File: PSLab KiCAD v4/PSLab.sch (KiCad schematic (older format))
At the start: 79 parts, among them CON1 USB-MINI-B, J1 Programmer, J10 GND, J11 Vbus, J12 Sensors, J13 D+, J14 D-, J2 SQRs, J3 LA, J4 OSC_Pins, J6 I2C, J7 IDs, J8 TX_RX_ES, J9 Test_Vs, P7 NRF, Q2 MMBT3904, Q3 MMBT3906, U1 MCP2200, U15 ESP8266, U2 74HC126, U3 PIC24EP256GP204, U4 TC1240A, U5 7660, U6 LM1117-3.3, X1 12MHz, Y1 12MHz

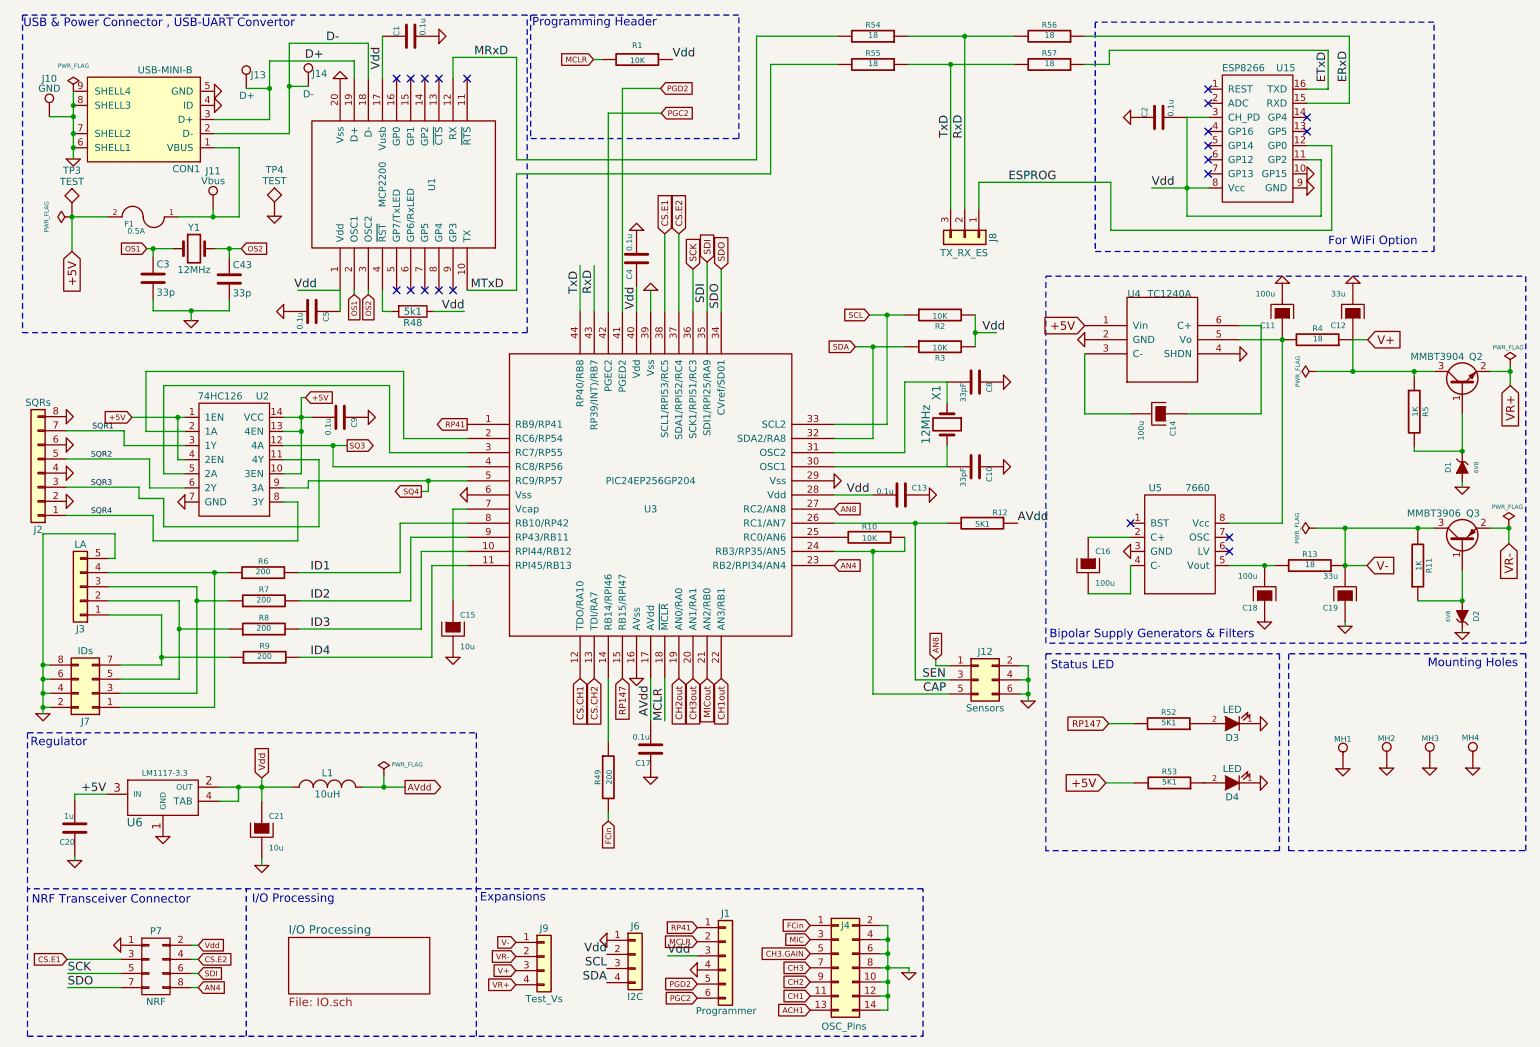
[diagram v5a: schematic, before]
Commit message: New layout with pins adjusted + Bluetooth
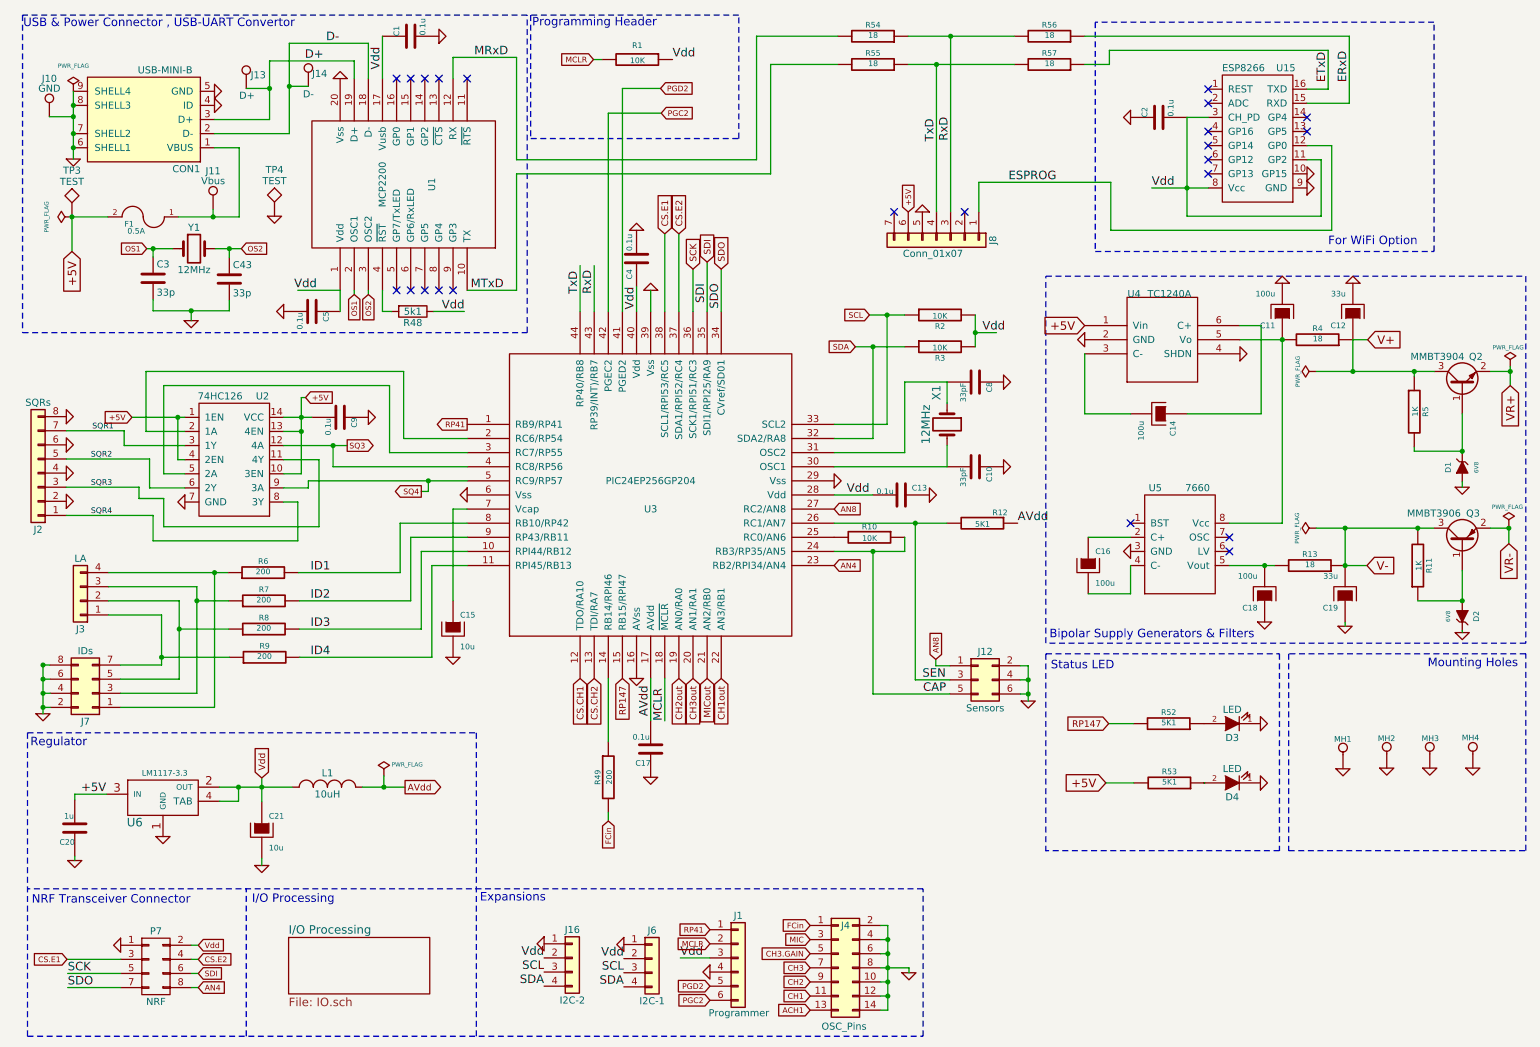
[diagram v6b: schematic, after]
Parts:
- removed J3: LA, Pin_Headers:Pin_Header_Straight_1x05_Pitch2.54mm, symbol Conn_01x05
- removed J8: TX_RX_ES, Pin_Headers:Pin_Header_Straight_1x03_Pitch2.54mm, symbol Conn_01x03
- removed J9: Test_Vs, Pin_Headers:Pin_Header_Straight_1x04_Pitch2.54mm, symbol Conn_01x04
- added J16: I2C-2, Pin_Headers:Pin_Header_Straight_1x04_Pitch2.54mm, symbol Conn_01x04
- added J3: LA, Pin_Headers:Pin_Header_Straight_1x04_Pitch2.54mm, symbol Conn_01x04
- added J8: Conn_01x07, Pin_Headers:Pin_Header_Straight_1x07_Pitch2.54mm, symbol Conn_01x07
- J6: value I2C -> I2C-1
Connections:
- net +5V: now also J8.6 (Pin_6)
- net ESPROG: now also J8.1 (Pin_1)
- net GND: now also J16.1 (Pin_1), J8.5 (Pin_5)
- net RxD: now also J8.3 (Pin_3)
- net SCL: now also J16.3 (Pin_3)
- net SDA: now also J16.4 (Pin_4)
- net TxD: now also J8.4 (Pin_4)
- net Vdd: now also J16.2 (Pin_2)
- net at J7.3 (Pin_3), R7.1: now also J3.3 (Pin_3)
- net at J7.1 (Pin_1), R6.1: now also J3.4 (Pin_4)
- net at J7.5 (Pin_5), R8.1: now also J3.2 (Pin_2)
- net at J7.7 (Pin_7), R9.1: now also J3.1 (Pin_1)
- no-connect marks 21 -> 23
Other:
- moved on the sheet: J1, J6
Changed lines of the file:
@@
 Text GLabel 6080 7150 0    40   Input ~ 0
 CH3.GAIN
-Text Label 4640 7355 2    60   ~ 0
+Text Label 4760 7385 2    60   ~ 0
 SDA
-Text Label 4640 7255 2    60   ~ 0
+Text Label 4760 7285 2    60   ~ 0
 SCL
 $Comp
 L GND-RESCUE-proto1 #PWR033
 U 1 1 55B40810
-P 4640 7055
-F 0 "#PWR033" H 4640 7055 30  0001 C CNN
-F 1 "GND" H 4640 6985 30  0001 C CNN
-F 2 "" H 4640 7055 60  0000 C CNN
-F 3 "" H 4640 7055 60  0000 C CNN
-	1    4640 7055
+P 4760 7085
+F 0 "#PWR033" H 4760 7085 30  0001 C CNN
+F 1 "GND" H 4760 7015 30  0001 C CNN
+F 2 "" H 4760 7085 60  0000 C CNN
+F 3 "" H 4760 7085 60  0000 C CNN
+	1    4760 7085
 	0    1    1    0
 $EndComp
-Text Label 4640 7155 2    60   ~ 0
-Vdd
 $Comp
 L Crystal X1
@@
 Text GLabel 5020 1020 2    40   Input ~ 0
 PGD2
-Text GLabel 5280 7365 0    40   Input ~ 0
+Text GLabel 5370 7380 0    40   Input ~ 0
 PGD2
-Text GLabel 5280 7465 0    40   Input ~ 0
+Text GLabel 5370 7480 0    40   Input ~ 0
 PGC2
 $Comp
@@
 Text GLabel 11040 3125 3    60   Input ~ 0
 VR+
-Text GLabel 5280 6965 0    40   Input ~ 0
+Text GLabel 5370 6980 0    40   Input ~ 0
 RP41
 Text GLabel 6970 5065 1    40   Input ~ 0
@@
 Text GLabel 3210 5970 2    47   Output ~ 0
 AVdd
-Text Label 7175 1375 1    60   ~ 0
+Text Label 7075 1390 1    60   ~ 0
 RxD
-Text Label 7075 1370 1    60   ~ 0
+Text Label 6975 1395 1    60   ~ 0
 TxD
 Text GLabel 3325 3875 0    40   Output ~ 0
@@
 	0    -1   -1   0
 $EndComp
-$Comp
-L Conn_01x03 J8
-U 1 1 5A320F8A
-P 7175 2075
-F 0 "J8" H 7175 2275 50  0000 C CNN
-F 1 "TX_RX_ES" V 7285 2070 50  0000 C CNN
-F 2 "Pin_Headers:Pin_Header_Straight_1x03_Pitch2.54mm" H 7175 2075 50  0001 C CNN
-F 3 "" H 7175 2075 50  0001 C CNN
-	1    7175 2075
-	0    1    1    0
-$EndComp
 Text Label 7485 1685 0    60   ~ 0
 ESPROG
@@
 L Conn_01x06 J1
 U 1 1 5A56B55E
-P 5480 7165
-F 0 "J1" H 5480 7465 50  0000 C CNN
-F 1 "Programmer" H 5485 6775 50  0000 C CNN
-F 2 "Pin_Headers:Pin_Header_Straight_1x06_Pitch2.54mm" H 5480 7165 50  0001 C CNN
-F 3 "" H 5480 7165 50  0001 C CNN
-	1    5480 7165
-	1    0    0    -1
-$EndComp
-Text Label 5070 7165 0    60   ~ 0
-Vdd
+P 5570 7180
+F 0 "J1" H 5570 7480 50  0000 C CNN
+F 1 "Programmer" H 5575 6790 50  0000 C CNN
+F 2 "Pin_Headers:Pin_Header_Straight_1x06_Pitch2.54mm" H 5570 7180 50  0001 C CNN
+F 3 "" H 5570 7180 50  0001 C CNN
+	1    5570 7180
+	1    0    0    -1
+$EndComp
 $Comp
 L GND-RESCUE-proto1 #PWR048
 U 1 1 5A56D115
-P 5280 7265
-F 0 "#PWR048" H 5280 7265 30  0001 C CNN
-F 1 "GND" H 5280 7195 30  0001 C CNN
-F 2 "" H 5280 7265 60  0000 C CNN
-F 3 "" H 5280 7265 60  0000 C CNN
-	1    5280 7265
+P 5370 7280
+F 0 "#PWR048" H 5370 7280 30  0001 C CNN
+F 1 "GND" H 5370 7210 30  0001 C CNN
+F 2 "" H 5370 7280 60  0000 C CNN
+F 3 "" H 5370 7280 60  0000 C CNN
+	1    5370 7280
 	0    1    1    0
 $EndComp
-Text GLabel 5280 7065 0    40   Input ~ 0
+Text GLabel 5370 7080 0    40   Input ~ 0
 MCLR
 Text GLabel 4545 815  0    40   Input ~ 0
@@
 L Conn_01x04 J6
 U 1 1 5A584DF9
-P 4840 7155
-F 0 "J6" H 4840 7355 50  0000 C CNN
-F 1 "I2C" H 4840 6855 50  0000 C CNN
-F 2 "Pin_Headers:Pin_Header_Straight_1x04_Pitch2.54mm" H 4840 7155 50  0001 C CNN
-F 3 "" H 4840 7155 50  0001 C CNN
-	1    4840 7155
+P 4960 7185
+F 0 "J6" H 4960 7385 50  0000 C CNN
+F 1 "I2C-1" H 4960 6885 50  0000 C CNN
+F 2 "Pin_Headers:Pin_Header_Straight_1x04_Pitch2.54mm" H 4960 7185 50  0001 C CNN
+F 3 "" H 4960 7185 50  0001 C CNN
+	1    4960 7185
 	1    0    0    -1
 $EndComp
@@
 	1    0    0    -1
 $EndComp
-$Comp
-L Conn_01x04 J9
-U 1 1 5A57CD2F
-P 4195 7170
-F 0 "J9" H 4195 7370 50  0000 C CNN
-F 1 "Test_Vs" H 4195 6870 50  0000 C CNN
-F 2 "Pin_Headers:Pin_Header_Straight_1x04_Pitch2.54mm" H 4195 7170 50  0001 C CNN
-F 3 "" H 4195 7170 50  0001 C CNN
-	1    4195 7170
-	1    0    0    -1
-$EndComp
-Text GLabel 3995 7070 0    40   Input ~ 0
-V-
-Text GLabel 3995 7170 0    40   Input ~ 0
-VR-
-Text GLabel 3995 7270 0    40   Input ~ 0
-V+
-Text GLabel 3995 7370 0    40   Input ~ 0
-VR+
-$Comp
-L Conn_01x05 J3
-U 1 1 5A595092
-P 910 4550
-F 0 "J3" H 910 4850 50  0000 C CNN
-F 1 "LA" H 910 4250 50  0000 C CNN
-F 2 "Pin_Headers:Pin_Header_Straight_1x05_Pitch2.54mm" H 910 4550 50  0001 C CNN
-F 3 "" H 910 4550 50  0001 C CNN
-	1    910  4550
-	-1   0    0    1
-$EndComp
 Wire Wire Line
 	3400 4400 3650 4400
@@
 	8175 5940 8375 5940
 Wire Wire Line
-	7275 1875 7275 1685
+	7275 1685 7275 1895
 Wire Wire Line
 	7275 1685 8210 1685
-Wire Wire Line
-	7175 1875 7175 650
-Connection ~ 7175 650
-Wire Wire Line
-	7075 1875 7075 850
-Connection ~ 7075 850
 Wire Notes Line
 	10500 550  8100 550
@@
 Wire Wire Line
 	6780 7250 6780 7285
-Wire Wire Line
-	5280 7165 5070 7165
 Wire Wire Line
 	4605 815  4545 815
@@
 	695  5405 645  5405
 Wire Wire Line
-	645  4175 645  5450
-Wire Wire Line
 	645  5105 695  5105
 Wire Wire Line
@@
 Connection ~ 645  5105
 Wire Wire Line
-	1110 4350 1155 4350
-Wire Wire Line
-	1155 4350 1155 4175
-Wire Wire Line
-	1155 4175 645  4175
-Wire Wire Line
 	1110 4450 1955 4450
 Wire Wire Line
@@
 	1485 5105 1195 5105
 Connection ~ 1485 5050
+Text Label 4760 7185 2    60   ~ 0
+Vdd
+Wire Wire Line
+	5370 7180 5160 7180
+Text Label 5160 7180 0    60   ~ 0
+Vdd
+$Comp
+L Conn_01x04 J16
+U 1 1 5AD47B2C
+P 4395 7180
+F 0 "J16" H 4395 7380 50  0000 C CNN
+F 1 "I2C-2" H 4395 6880 50  0000 C CNN
+F 2 "Pin_Headers:Pin_Header_Straight_1x04_Pitch2.54mm" H 4395 7180 50  0001 C CNN
+F 3 "" H 4395 7180 50  0001 C CNN
+	1    4395 7180
+	1    0    0    -1
+$EndComp
+$Comp
+L GND-RESCUE-proto1 #PWR059
+U 1 1 5AD48170
+P 4195 7080
+F 0 "#PWR059" H 4195 7080 30  0001 C CNN
+F 1 "GND" H 4195 7010 30  0001 C CNN
+F 2 "" H 4195 7080 60  0000 C CNN
+F 3 "" H 4195 7080 60  0000 C CNN
+	1    4195 7080
+	0    1    1    0
+$EndComp
+Text Label 4195 7180 2    60   ~ 0
+Vdd
+Text Label 4195 7280 2    60   ~ 0
+SCL
+Text Label 4195 7380 2    60   ~ 0
+SDA
+$Comp
+L Conn_01x07 J8
+U 1 1 5AD486BC
+P 6975 2095
+F 0 "J8" H 6975 2495 50  0000 C CNN
+F 1 "Conn_01x07" V 7070 2070 50  0000 C CNN
+F 2 "Pin_Headers:Pin_Header_Straight_1x07_Pitch2.54mm" H 6975 2095 50  0001 C CNN
+F 3 "" H 6975 2095 50  0001 C CNN
+	1    6975 2095
+	0    1    1    0
+$EndComp
+Wire Wire Line
+	6975 1895 6975 850
+Connection ~ 6975 850
+Wire Wire Line
+	7075 1895 7075 650
+Connection ~ 7075 650
+$Comp
+L GND-RESCUE-proto1 #PWR060
+U 1 1 5AD4BD5F
+P 6875 1895
+F 0 "#PWR060" H 6875 1895 30  0001 C CNN
+F 1 "GND" H 6875 1825 30  0001 C CNN
+F 2 "" H 6875 1895 60  0000 C CNN
+F 3 "" H 6875 1895 60  0000 C CNN
+	1    6875 1895
+	-1   0    0    1
+$EndComp
+Text GLabel 6775 1895 1    40   Input ~ 0
++5V
+NoConn ~ 7175 1895
+NoConn ~ 6675 1895
+$Comp
+L Conn_01x04 J3
+U 1 1 5AD4C0DD
+P 910 4650
+F 0 "J3" H 910 4850 50  0000 C CNN
+F 1 "LA" H 910 4350 50  0000 C CNN
+F 2 "Pin_Headers:Pin_Header_Straight_1x04_Pitch2.54mm" H 910 4650 50  0001 C CNN
+F 3 "" H 910 4650 50  0001 C CNN
+	1    910  4650
+	-1   0    0    1
+$EndComp
+Wire Wire Line
+	645  5105 645  5450
 $EndSCHEMATC

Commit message: Modifications to PSLab PCB (#39)
* Refined BOM Sheet

* Added FOSSASIA Logo and updated BoM

* NRF replaced with Bluetooth

* Modified silk screen texts
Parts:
- removed C15, C21: 10u, Capacitors_SMD:C_0603, symbol CAPAPOL
- removed J12: Sensors, Pin_Headers:Pin_Header_Straight_2x03_Pitch2.54mm, symbol Conn_02x03_Odd_Even
- removed J2: SQRs, Pin_Headers:Pin_Header_Straight_1x08_Pitch2.54mm, symbol Conn_01x08
- removed J4: OSC_Pins, Pin_Headers:Pin_Header_Straight_2x07_Pitch2.54mm, symbol Conn_02x07_Odd_Even
- removed J7: IDs, Pin_Headers:Pin_Header_Straight_2x04_Pitch2.54mm, symbol Conn_02x04_Odd_Even
- removed J8: Conn_01x07, Pin_Headers:Pin_Header_Straight_1x07_Pitch2.54mm, symbol Conn_01x07
- removed P7: NRF, Pin_Headers:Pin_Header_Straight_2x04_Pitch2.54mm, symbol CONN_02X04
- added C15, C21: 10u, Capacitors_SMD:C_0603, symbol C-RESCUE-proto1
- added J2: DoublePins, Pin_Headers:Pin_Header_Straight_2x14_Pitch2.54mm, symbol Conn_02x14_Odd_Even
- added J5: Bluetooth, Pin_Headers:Pin_Header_Straight_1x06_Pitch2.54mm, symbol Conn_01x06
- added J7: UART/ESP, Pin_Headers:Pin_Header_Straight_1x07_Pitch2.54mm, symbol Conn_01x07
- C10, C8: value 33pF -> 33p
- C3, C43: symbol C -> C-RESCUE-proto1
- MH1, MH2, MH3, MH4: footprint Mounting_Holes:MountingHole_2.2mm_M2_ISO14580_Pad -> Mounting_Holes:MountingHole_3.2mm_M3_DIN965_Pad
- R48: value 5k1 -> 5K1; symbol R -> R-RESCUE-proto1
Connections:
- net +5V: now also J5.2 (Pin_2), J7.6 (Pin_6)
- net ACH1: now also J2.19 (Pin_19)
- net AN8: now also J2.1 (Pin_1)
- net CAP: now also J2.5 (Pin_5)
- net CH1: now also J2.17 (Pin_17)
- net CH2: now also J2.15 (Pin_15)
- net CH3: now also J2.13 (Pin_13)
- net CH3.GAIN: now also J2.11 (Pin_11)
- net ESPROG: now also J7.2 (Pin_2)
- net FCin: now also J2.7 (Pin_7)
- net GND: now also J1.3 (Pin_3), C15.1, C21.1, J2.10 (Pin_10), J2.12 (Pin_12), J2.14 (Pin_14), J2.16 (Pin_16), J2.18 (Pin_18), J2.2 (Pin_2), J2.20 (Pin_20), J2.22 (Pin_22), J2.24 (Pin_24), J2.26 (Pin_26), J2.28 (Pin_28), J2.4 (Pin_4), J2.6 (Pin_6), J2.8 (Pin_8), J5.3 (Pin_3), J7.1 (Pin_1), J7.5 (Pin_5); no longer J1.4 (Pin_4)
- net MCLR: now also J1.1 (Pin_1); no longer J1.2 (Pin_2)
- net MIC: now also J2.9 (Pin_9)
- net PGC2: now also J1.5 (Pin_5); no longer J1.6 (Pin_6)
- net PGD2: now also J1.4 (Pin_4); no longer J1.5 (Pin_5)
- net RxD: now also J5.5 (Pin_5), J7.3 (Pin_3)
- net SEN: now also J2.3 (Pin_3)
- net TxD: now also J5.4 (Pin_4), J7.4 (Pin_4)
- net Vdd: now also J1.2 (Pin_2), C15.2, J7.7 (Pin_7); no longer J1.3 (Pin_3)
- net IDB: now reaches J3.3 (Pin_3), R7.1
- net IDB: now also J2.25 (Pin_25)
- net IDA: now reaches J3.4 (Pin_4), R6.1
- net IDA: now also J2.27 (Pin_27)
- net at U3.7 (Vcap): now also C21.2
- net IDC: now reaches J3.2 (Pin_2), R8.1
- net IDC: now also J2.23 (Pin_23)
- net IDD: now reaches J3.1 (Pin_1), R9.1
- net IDD: now also J2.21 (Pin_21)
- net AN4: no longer names the net of U3.23 (RB2/RPI34/AN4)
- net CS.E1: no longer names the net of U3.38 (SCL1/RPI53/RC5)
- net CS.E2: no longer names the net of U3.37 (SDA1/RPI52/RC4)
- net RP41: no longer names the net of U3.1 (RB9/RP41)
- net RP41: no longer J1.1 (Pin_1)
- net SDI: no longer names the net of U3.35 (SDI1/RPI25/RA9)
- no-connect marks 23 -> 29
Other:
- note added: "Bluetooth"
- note added: "Logic Analyzer"
- note removed: "NRF Transceiver Connector"
- moved on the sheet: J3, R48
